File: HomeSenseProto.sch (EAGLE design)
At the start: 20 parts, among them IC1 ESP12SMT

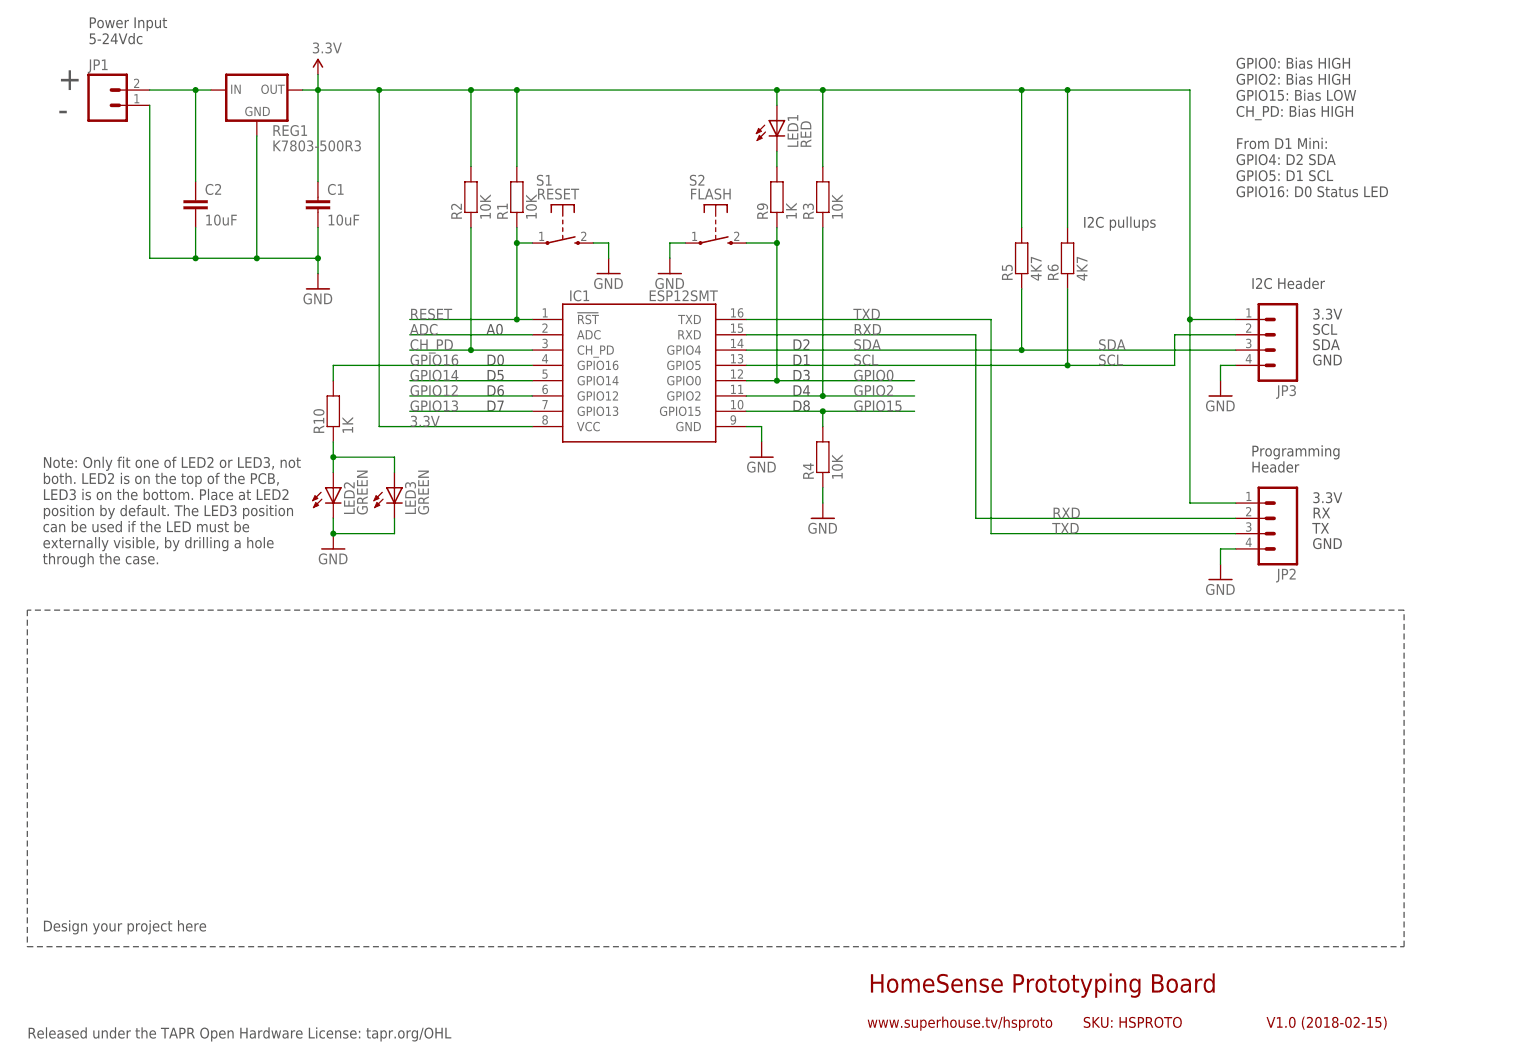
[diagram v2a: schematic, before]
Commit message: Added more IO pins to breakout area
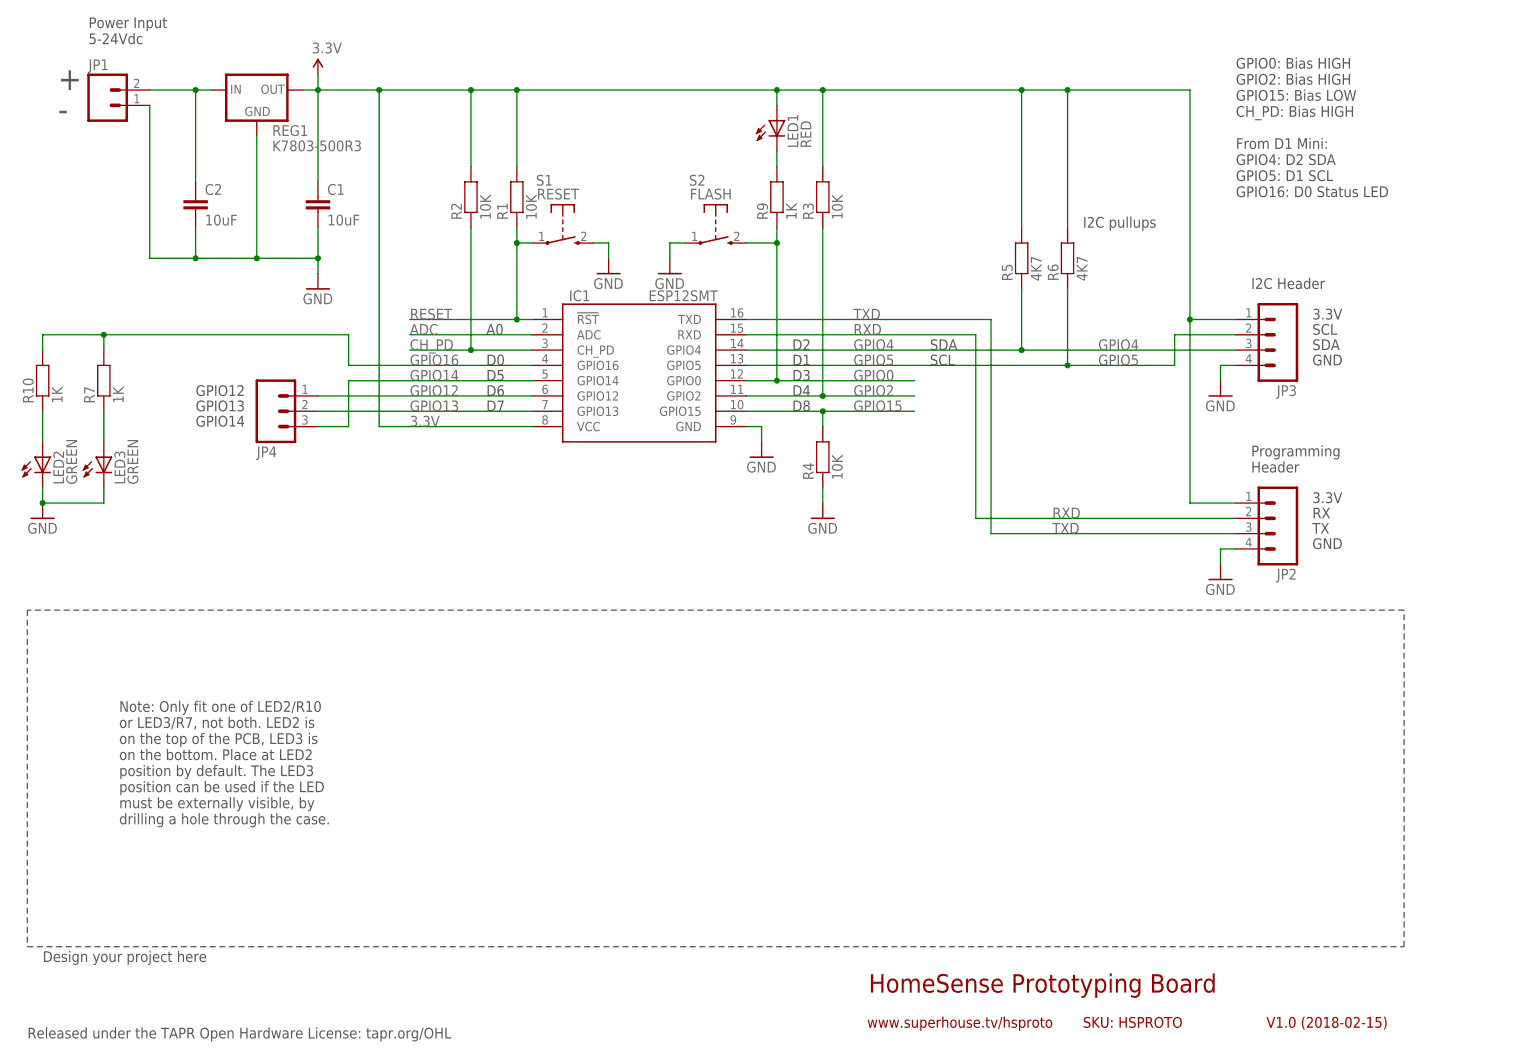
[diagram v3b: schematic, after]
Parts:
- added JP4: (no value), freetronics-jon:M03PTH
- added R7: 1K, freetronics-jon:RESISTOR0603
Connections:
- net SCL renamed GPIO5
- net SDA renamed GPIO4
- new net N$64: LED2.A, R10.1
- net GPIO12: now also JP4.1
- net GPIO13: now also JP4.2
- net GPIO14: now also JP4.3
- net GPIO16: now also R7.2
- net N$11: now also R7.1; no longer LED2.A, R10.1
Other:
- note added: "GPIO12"
- note added: "GPIO13"
- note added: "GPIO14"
- note added: "Note: Only fit one of LED2/R10 or LED3/R7, not both. LED2 is on the top of the PCB, LED3 is on the bottom. Place at LED2 position by default. The LED3 position can be used if the LED must be externally visible, by drilling a hole through the case."
- note removed: "Note: Only fit one of LED2 or LED3, not both. LED2 is on the top of the PCB, LED3 is on the bottom. Place at LED2 position by default. The LED3 position can be used if the LED must be externally visible, by drilling a hole through the case."
- moved on the sheet: LED2, LED3, R10
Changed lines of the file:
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@@
 <part name="JP3" library="freetronics-jon" deviceset="M04" device="PTH"/>
 <part name="LED3" library="freetronics-jon" deviceset="LED" device="0603" value="GREEN"/>
+<part name="R7" library="freetronics-jon" deviceset="RESISTOR" device="0603" value="1K"/>
+<part name="JP4" library="freetronics-jon" deviceset="M03" device="PTH"/>
 </parts>
 <sheets>
@@
 <frame x1="213.36" y1="5.08" x2="243.84" y2="10.16" columns="8" rows="5" layer="94"/>
 <text x="10.16" y="5.08" size="1.778" layer="97">Released under the TAPR Open Hardware License: tapr.org/OHL</text>
-<text x="12.7" y="22.86" size="1.778" layer="97">Design your project here</text>
+<text x="12.7" y="17.78" size="1.778" layer="97">Design your project here</text>
 <text x="210.82" y="144.78" size="1.778" layer="97">GPIO0: Bias HIGH
 GPIO2: Bias HIGH
@@
 <wire x1="238.76" y1="76.2" x2="10.16" y2="76.2" width="0.1524" layer="97" style="longdash"/>
 <wire x1="10.16" y1="76.2" x2="10.16" y2="20.32" width="0.1524" layer="97" style="longdash"/>
-<text x="12.7" y="83.82" size="1.778" layer="97">Note: Only fit one of LED2 or LED3, not
-both. LED2 is on the top of the PCB,
-LED3 is on the bottom. Place at LED2
-position by default. The LED3 position
-can be used if the LED must be
-externally visible, by drilling a hole
-through the case.</text>
+<text x="25.4" y="40.64" size="1.778" layer="97">Note: Only fit one of LED2/R10
+or LED3/R7, not both. LED2 is
+on the top of the PCB, LED3 is
+on the bottom. Place at LED2
+position by default. The LED3
+position can be used if the LED
+must be externally visible, by
+drilling a hole through the case.</text>
 <text x="86.36" y="116.84" size="1.778" layer="97">D0</text>
 <text x="86.36" y="114.3" size="1.778" layer="97">D5</text>
@@
 <frame x1="182.88" y1="5.08" x2="213.36" y2="10.16" columns="8" rows="5" layer="94"/>
 <text x="185.42" y="6.858" size="1.778" layer="94">SKU: HSPROTO</text>
+<text x="38.1" y="106.68" size="1.778" layer="97">GPIO14</text>
+<text x="38.1" y="111.76" size="1.778" layer="97">GPIO12</text>
+<text x="38.1" y="109.22" size="1.778" layer="97">GPIO13</text>
+<text x="160.02" y="116.84" size="1.778" layer="97">SCL</text>
+<text x="160.02" y="119.38" size="1.778" layer="97">SDA</text>
 </plain>
 <instances>
@@
 <instance part="R9" gate="G$1" x="134.62" y="144.78" rot="R90"/>
 <instance part="C2" gate="G$1" x="38.1" y="142.24"/>
-<instance part="R10" gate="G$1" x="60.96" y="109.22" rot="R90"/>
-<instance part="LED2" gate="G$1" x="60.96" y="96.52"/>
-<instance part="GND11" gate="1" x="60.96" y="86.36"/>
+<instance part="R10" gate="G$1" x="12.7" y="114.3" rot="R90"/>
+<instance part="LED2" gate="G$1" x="12.7" y="101.6"/>
+<instance part="GND11" gate="1" x="12.7" y="91.44"/>
 <instance part="JP1" gate="G$1" x="22.86" y="160.02"/>
 <instance part="JP2" gate="G$1" x="215.9" y="91.44" rot="R180"/>
@@
 <instance part="GND2" gate="1" x="116.84" y="132.08"/>
 <instance part="JP3" gate="G$1" x="215.9" y="121.92" rot="R180"/>
-<instance part="LED3" gate="G$1" x="71.12" y="96.52"/>
+<instance part="LED3" gate="G$1" x="22.86" y="101.6"/>
+<instance part="R7" gate="G$1" x="22.86" y="114.3" rot="R90"/>
+<instance part="JP4" gate="G$1" x="50.8" y="109.22" rot="MR180"/>
 </instances>
 <busses>
@@
 <pinref part="LED2" gate="G$1" pin="C"/>
 <pinref part="GND11" gate="1" pin="GND"/>
-<wire x1="60.96" y1="88.9" x2="60.96" y2="91.44" width="0.1524" layer="91"/>
+<wire x1="12.7" y1="93.98" x2="12.7" y2="96.52" width="0.1524" layer="91"/>
 <pinref part="LED3" gate="G$1" pin="C"/>
-<wire x1="71.12" y1="91.44" x2="71.12" y2="88.9" width="0.1524" layer="91"/>
-<wire x1="71.12" y1="88.9" x2="60.96" y2="88.9" width="0.1524" layer="91"/>
-<junction x="60.96" y="88.9"/>
+<wire x1="22.86" y1="96.52" x2="22.86" y2="93.98" width="0.1524" layer="91"/>
+<wire x1="22.86" y1="93.98" x2="12.7" y2="93.98" width="0.1524" layer="91"/>
+<junction x="12.7" y="93.98"/>
 </segment>
 <segment>
@@
 <segment>
 <pinref part="IC1" gate="G$1" pin="GPIO16"/>
-<wire x1="60.96" y1="116.84" x2="93.98" y2="116.84" width="0.1524" layer="91"/>
+<wire x1="12.7" y1="121.92" x2="22.86" y2="121.92" width="0.1524" layer="91"/>
 <pinref part="R10" gate="G$1" pin="2"/>
-<wire x1="60.96" y1="114.3" x2="60.96" y2="116.84" width="0.1524" layer="91"/>
+<wire x1="22.86" y1="121.92" x2="63.5" y2="121.92" width="0.1524" layer="91"/>
+<wire x1="63.5" y1="121.92" x2="63.5" y2="116.84" width="0.1524" layer="91"/>
+<wire x1="63.5" y1="116.84" x2="93.98" y2="116.84" width="0.1524" layer="91"/>
+<wire x1="12.7" y1="119.38" x2="12.7" y2="121.92" width="0.1524" layer="91"/>
 <label x="73.66" y="116.84" size="1.778" layer="95"/>
-</segment>
-</net>
-<net name="GPIO14" class="0">
-<segment>
-<pinref part="IC1" gate="G$1" pin="GPIO14"/>
-<wire x1="73.66" y1="114.3" x2="93.98" y2="114.3" width="0.1524" layer="91"/>
-<label x="73.66" y="114.3" size="1.778" layer="95"/>
-</segment>
-</net>
-<net name="GPIO12" class="0">
-<segment>
-<pinref part="IC1" gate="G$1" pin="GPIO12"/>
-<wire x1="73.66" y1="111.76" x2="93.98" y2="111.76" width="0.1524" layer="91"/>
-<label x="73.66" y="111.76" size="1.778" layer="95"/>
-</segment>
-</net>
-<net name="GPIO13" class="0">
-<segment>
-<pinref part="IC1" gate="G$1" pin="GPIO13"/>
-<wire x1="73.66" y1="109.22" x2="93.98" y2="109.22" width="0.1524" layer="91"/>
-<label x="73.66" y="109.22" size="1.778" layer="95"/>
+<pinref part="R7" gate="G$1" pin="2"/>
+<wire x1="22.86" y1="119.38" x2="22.86" y2="121.92" width="0.1524" layer="91"/>
+<junction x="22.86" y="121.92"/>
 </segment>
 </net>
@@
 </segment>
 </net>
-<net name="SDA" class="0">
+<net name="GPIO4" class="0">
 <segment>
 <pinref part="IC1" gate="G$1" pin="GPIO4"/>
@@
 </segment>
 </net>
-<net name="SCL" class="0">
+<net name="GPIO5" class="0">
 <segment>
 <pinref part="IC1" gate="G$1" pin="GPIO5"/>
@@
 <net name="N$11" class="0">
 <segment>
-<pinref part="R10" gate="G$1" pin="1"/>
-<pinref part="LED2" gate="G$1" pin="A"/>
-<wire x1="60.96" y1="99.06" x2="60.96" y2="101.6" width="0.1524" layer="91"/>
 <pinref part="LED3" gate="G$1" pin="A"/>
-<wire x1="60.96" y1="101.6" x2="60.96" y2="104.14" width="0.1524" layer="91"/>
-<wire x1="60.96" y1="101.6" x2="71.12" y2="101.6" width="0.1524" layer="91"/>
-<wire x1="71.12" y1="101.6" x2="71.12" y2="99.06" width="0.1524" layer="91"/>
-<junction x="60.96" y="101.6"/>
+<pinref part="R7" gate="G$1" pin="1"/>
+<wire x1="22.86" y1="109.22" x2="22.86" y2="104.14" width="0.1524" layer="91"/>
 </segment>
 </net>
@@
 </segment>
 </net>
+<net name="N$64" class="0">
+<segment>
+<pinref part="R10" gate="G$1" pin="1"/>
+<pinref part="LED2" gate="G$1" pin="A"/>
+<wire x1="12.7" y1="104.14" x2="12.7" y2="109.22" width="0.1524" layer="91"/>
+</segment>
+</net>
+<net name="GPIO13" class="0">
+<segment>
+<pinref part="IC1" gate="G$1" pin="GPIO13"/>
+<pinref part="JP4" gate="G$1" pin="2"/>
+<wire x1="93.98" y1="109.22" x2="58.42" y2="109.22" width="0.1524" layer="91"/>
+<label x="73.66" y="109.22" size="1.778" layer="95"/>
+</segment>
+</net>
+<net name="GPIO12" class="0">
+<segment>
+<pinref part="IC1" gate="G$1" pin="GPIO12"/>
+<pinref part="JP4" gate="G$1" pin="1"/>
+<wire x1="93.98" y1="111.76" x2="58.42" y2="111.76" width="0.1524" layer="91"/>
+<label x="73.66" y="111.76" size="1.778" layer="95"/>
+</segment>
+</net>
+<net name="GPIO14" class="0">
+<segment>
+<pinref part="IC1" gate="G$1" pin="GPIO14"/>
+<wire x1="93.98" y1="114.3" x2="63.5" y2="114.3" width="0.1524" layer="91"/>
+<wire x1="63.5" y1="114.3" x2="63.5" y2="106.68" width="0.1524" layer="91"/>
+<pinref part="JP4" gate="G$1" pin="3"/>
+<wire x1="63.5" y1="106.68" x2="58.42" y2="106.68" width="0.1524" layer="91"/>
+<label x="73.66" y="114.3" size="1.778" layer="95"/>
+</segment>
+</net>
